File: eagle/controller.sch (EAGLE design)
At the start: 18 parts, among them IC2 74HCT595N

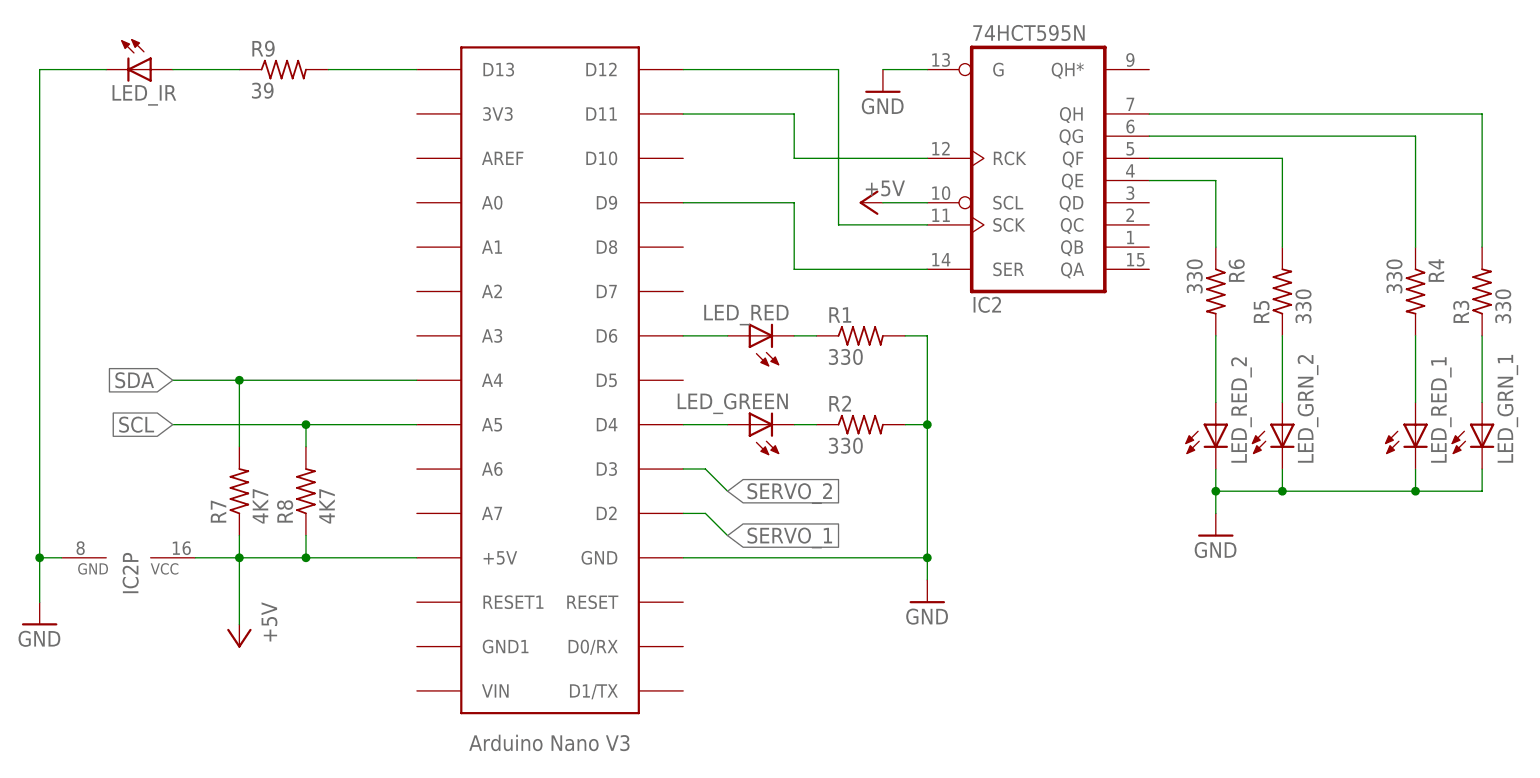
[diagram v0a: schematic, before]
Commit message: Clarify servo connections in schematic
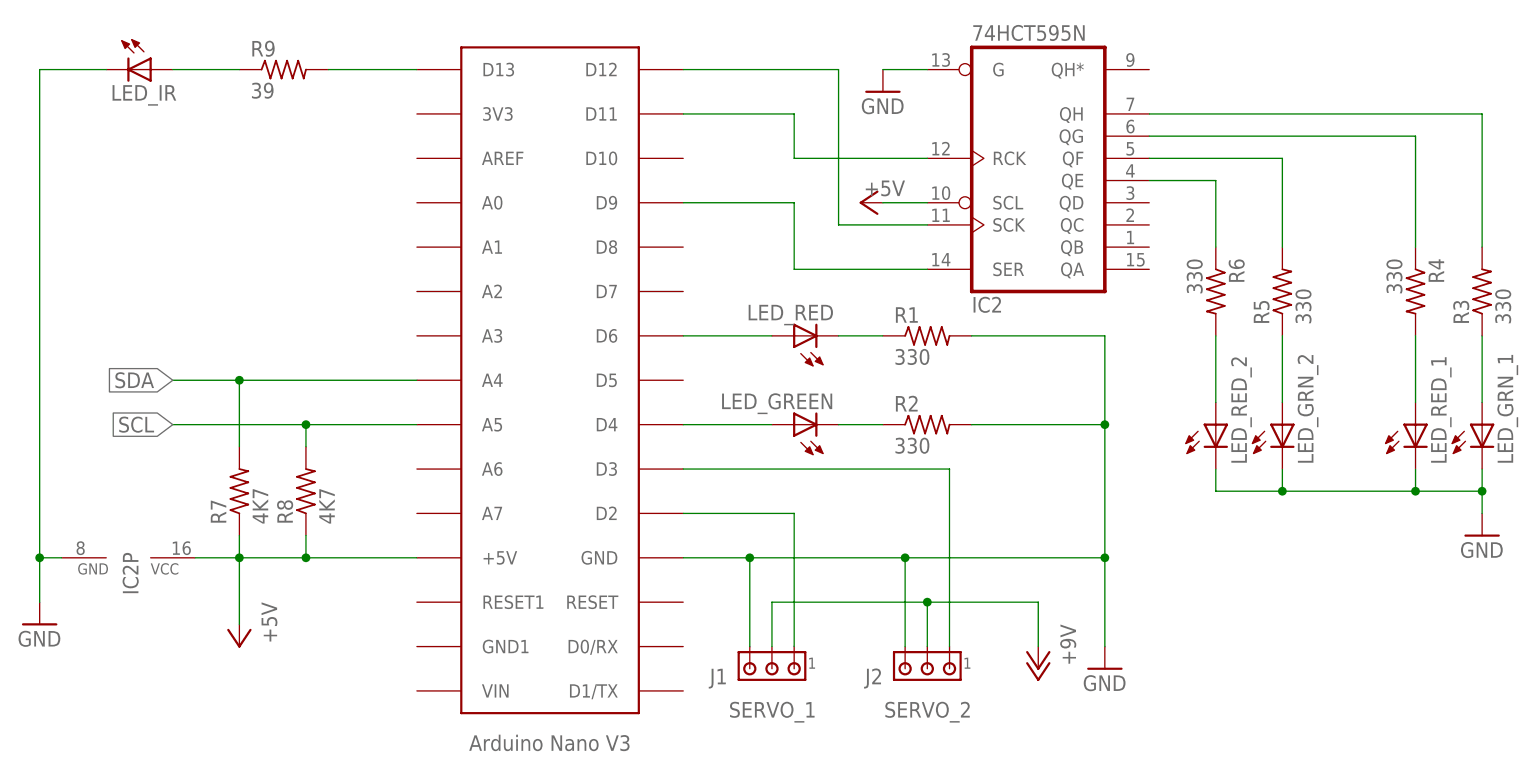
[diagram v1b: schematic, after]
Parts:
- added J1: SERVO_1, con-amp:MTA03-100
- added J2: SERVO_2, con-amp:MTA03-100
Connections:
- removed net SERVO_1: U$1.D2
- removed net SERVO_2: U$1.D3
- new net +12V: J1.2, J2.2
- new net N$18: J1.1, U$1.D2
- new net N$19: J2.1, U$1.D3
- net GND: now also J1.3, J2.3
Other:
- moved on the sheet: LED_GREEN, LED_RED, R1, R2
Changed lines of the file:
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@@
 <part name="R8" library="resistor" deviceset="R-US_" device="0207/10" value="4K7"/>
 <part name="P+1" library="supply1" deviceset="+5V" device=""/>
-<part name="GND3" library="supply1" deviceset="GND" device=""/>
 <part name="R9" library="resistor" deviceset="R-US_" device="0207/10" value="39"/>
 <part name="LED_IR" library="led" deviceset="LED" device="5MM"/>
@@
 <part name="GND1" library="supply1" deviceset="GND" device=""/>
 <part name="GND2" library="supply1" deviceset="GND" device=""/>
+<part name="J1" library="con-amp" deviceset="MTA03-100" device="" value="SERVO_1"/>
+<part name="J2" library="con-amp" deviceset="MTA03-100" device="" value="SERVO_2"/>
+<part name="P+3" library="supply1" deviceset="+12V" device="" value="+9V"/>
+<part name="GND4" library="supply1" deviceset="GND" device=""/>
 </parts>
 <sheets>
@@
 <attribute name="VALUE" x="-2.54" y="48.26" size="1.778" layer="96" rot="R180"/>
 </instance>
-<instance part="LED_GREEN" gate="G$1" x="-20.32" y="20.32" rot="R90"/>
-<instance part="LED_RED" gate="G$1" x="-20.32" y="30.48" rot="R90"/>
-<instance part="R1" gate="G$1" x="-7.62" y="30.48"/>
-<instance part="R2" gate="G$1" x="-7.62" y="20.32"/>
+<instance part="LED_GREEN" gate="G$1" x="-15.24" y="20.32" rot="R90"/>
+<instance part="LED_RED" gate="G$1" x="-15.24" y="30.48" rot="R90"/>
+<instance part="R1" gate="G$1" x="0" y="30.48"/>
+<instance part="R2" gate="G$1" x="0" y="20.32"/>
 <instance part="R3" gate="G$1" x="63.5" y="35.56" rot="R90"/>
 <instance part="R4" gate="G$1" x="55.88" y="35.56" rot="R270"/>
@@
 <instance part="R8" gate="G$1" x="-71.12" y="12.7" rot="R90"/>
 <instance part="P+1" gate="1" x="-78.74" y="-5.08" rot="R180"/>
-<instance part="GND3" gate="1" x="0" y="0"/>
 <instance part="R9" gate="G$1" x="-73.66" y="60.96"/>
 <instance part="LED_IR" gate="G$1" x="-88.9" y="60.96" rot="R270"/>
@@
 <instance part="LED_GRN_1" gate="G$1" x="63.5" y="20.32"/>
 <instance part="LED_GRN_2" gate="G$1" x="40.64" y="20.32"/>
-<instance part="GND5" gate="1" x="33.02" y="7.62"/>
+<instance part="GND5" gate="1" x="63.5" y="7.62"/>
 <instance part="IC2" gate="A" x="12.7" y="48.26" rot="MR180"/>
 <instance part="GND1" gate="1" x="-5.08" y="58.42"/>
 <instance part="IC2" gate="P" x="-91.44" y="5.08" rot="R270"/>
 <instance part="GND2" gate="1" x="-101.6" y="-2.54"/>
+<instance part="J1" gate="G$1" x="-17.78" y="-7.62" smashed="yes" rot="R180">
+<attribute name="NAME" x="-22.86" y="-7.62" size="1.778" layer="95" rot="R180"/>
+<attribute name="VALUE" x="-12.7" y="-11.43" size="1.778" layer="96" rot="R180"/>
+</instance>
+<instance part="J2" gate="G$1" x="0" y="-7.62" smashed="yes" rot="R180">
+<attribute name="NAME" x="-5.08" y="-7.62" size="1.778" layer="95" rot="R180"/>
+<attribute name="VALUE" x="5.08" y="-11.43" size="1.778" layer="96" rot="R180"/>
+</instance>
+<instance part="P+3" gate="1" x="12.7" y="-7.62" rot="R180"/>
+<instance part="GND4" gate="1" x="20.32" y="-7.62"/>
 </instances>
 <busses>
@@
 </net>
 <net name="GND" class="0">
-<segment>
-<pinref part="R1" gate="G$1" pin="2"/>
-<wire x1="-2.54" y1="30.48" x2="0" y2="30.48" width="0.1524" layer="91"/>
-<wire x1="0" y1="30.48" x2="0" y2="20.32" width="0.1524" layer="91"/>
-<pinref part="GND3" gate="1" pin="GND"/>
-<pinref part="R2" gate="G$1" pin="2"/>
-<wire x1="0" y1="20.32" x2="0" y2="5.08" width="0.1524" layer="91"/>
-<wire x1="0" y1="5.08" x2="0" y2="2.54" width="0.1524" layer="91"/>
-<wire x1="-2.54" y1="20.32" x2="0" y2="20.32" width="0.1524" layer="91"/>
-<junction x="0" y="20.32"/>
-<pinref part="U$1" gate="G$1" pin="GND"/>
-<wire x1="-27.94" y1="5.08" x2="0" y2="5.08" width="0.1524" layer="91"/>
-<junction x="0" y="5.08"/>
-</segment>
 <segment>
 <pinref part="LED_IR" gate="G$1" pin="C"/>
@@
 <wire x1="-101.6" y1="5.08" x2="-101.6" y2="0" width="0.1524" layer="91"/>
 <junction x="-101.6" y="5.08"/>
+</segment>
+<segment>
+<pinref part="IC2" gate="A" pin="G"/>
+<wire x1="0" y1="60.96" x2="-5.08" y2="60.96" width="0.1524" layer="91"/>
+<pinref part="GND1" gate="1" pin="GND"/>
+</segment>
+<segment>
+<pinref part="U$1" gate="G$1" pin="GND"/>
+<pinref part="J1" gate="G$1" pin="3"/>
+<wire x1="-20.32" y1="-5.08" x2="-20.32" y2="5.08" width="0.1524" layer="91"/>
+<wire x1="-20.32" y1="5.08" x2="-27.94" y2="5.08" width="0.1524" layer="91"/>
+<pinref part="J2" gate="G$1" pin="3"/>
+<wire x1="-2.54" y1="-5.08" x2="-2.54" y2="5.08" width="0.1524" layer="91"/>
+<wire x1="-2.54" y1="5.08" x2="-20.32" y2="5.08" width="0.1524" layer="91"/>
+<junction x="-20.32" y="5.08"/>
+<wire x1="-2.54" y1="5.08" x2="20.32" y2="5.08" width="0.1524" layer="91"/>
+<junction x="-2.54" y="5.08"/>
+<wire x1="20.32" y1="5.08" x2="20.32" y2="-5.08" width="0.1524" layer="91"/>
+<pinref part="GND4" gate="1" pin="GND"/>
+<pinref part="R1" gate="G$1" pin="2"/>
+<wire x1="5.08" y1="30.48" x2="20.32" y2="30.48" width="0.1524" layer="91"/>
+<wire x1="20.32" y1="30.48" x2="20.32" y2="20.32" width="0.1524" layer="91"/>
+<pinref part="R2" gate="G$1" pin="2"/>
+<wire x1="5.08" y1="20.32" x2="20.32" y2="20.32" width="0.1524" layer="91"/>
+<wire x1="20.32" y1="20.32" x2="20.32" y2="5.08" width="0.1524" layer="91"/>
+<junction x="20.32" y="20.32"/>
+<junction x="20.32" y="5.08"/>
 </segment>
 <segment>
@@
 <junction x="40.64" y="12.7"/>
 <pinref part="GND5" gate="1" pin="GND"/>
-<wire x1="33.02" y1="12.7" x2="33.02" y2="10.16" width="0.1524" layer="91"/>
-<junction x="33.02" y="12.7"/>
-</segment>
-<segment>
-<pinref part="IC2" gate="A" pin="G"/>
-<wire x1="0" y1="60.96" x2="-5.08" y2="60.96" width="0.1524" layer="91"/>
-<pinref part="GND1" gate="1" pin="GND"/>
+<wire x1="63.5" y1="10.16" x2="63.5" y2="12.7" width="0.1524" layer="91"/>
+<junction x="63.5" y="12.7"/>
 </segment>
 </net>
@@
 <pinref part="U$1" gate="G$1" pin="D4"/>
 <pinref part="LED_GREEN" gate="G$1" pin="A"/>
-<wire x1="-27.94" y1="20.32" x2="-22.86" y2="20.32" width="0.1524" layer="91"/>
+<wire x1="-27.94" y1="20.32" x2="-17.78" y2="20.32" width="0.1524" layer="91"/>
 </segment>
 </net>
@@
 <pinref part="U$1" gate="G$1" pin="D6"/>
 <pinref part="LED_RED" gate="G$1" pin="A"/>
-<wire x1="-27.94" y1="30.48" x2="-22.86" y2="30.48" width="0.1524" layer="91"/>
+<wire x1="-27.94" y1="30.48" x2="-17.78" y2="30.48" width="0.1524" layer="91"/>
 </segment>
 </net>
@@
 <pinref part="LED_RED" gate="G$1" pin="C"/>
 <pinref part="R1" gate="G$1" pin="1"/>
-<wire x1="-15.24" y1="30.48" x2="-12.7" y2="30.48" width="0.1524" layer="91"/>
+<wire x1="-10.16" y1="30.48" x2="-5.08" y2="30.48" width="0.1524" layer="91"/>
 </segment>
 </net>
@@
 <pinref part="LED_GREEN" gate="G$1" pin="C"/>
 <pinref part="R2" gate="G$1" pin="1"/>
-<wire x1="-15.24" y1="20.32" x2="-12.7" y2="20.32" width="0.1524" layer="91"/>
+<wire x1="-10.16" y1="20.32" x2="-5.08" y2="20.32" width="0.1524" layer="91"/>
 </segment>
 </net>
@@
 </segment>
 </net>
-<net name="SERVO_2" class="0">
-<segment>
-<pinref part="U$1" gate="G$1" pin="D3"/>
-<wire x1="-27.94" y1="15.24" x2="-25.4" y2="15.24" width="0.1524" layer="91"/>
-<wire x1="-25.4" y1="15.24" x2="-22.86" y2="12.7" width="0.1524" layer="91"/>
-<label x="-22.86" y="12.7" size="1.778" layer="95" xref="yes"/>
-</segment>
-</net>
-<net name="SERVO_1" class="0">
-<segment>
-<pinref part="U$1" gate="G$1" pin="D2"/>
-<wire x1="-27.94" y1="10.16" x2="-25.4" y2="10.16" width="0.1524" layer="91"/>
-<wire x1="-25.4" y1="10.16" x2="-22.86" y2="7.62" width="0.1524" layer="91"/>
-<label x="-22.86" y="7.62" size="1.778" layer="95" xref="yes"/>
-</segment>
-</net>
 <net name="N$8" class="0">
 <segment>
@@
 </segment>
 </net>
+<net name="N$18" class="0">
+<segment>
+<pinref part="U$1" gate="G$1" pin="D2"/>
+<wire x1="-27.94" y1="10.16" x2="-15.24" y2="10.16" width="0.1524" layer="91"/>
+<pinref part="J1" gate="G$1" pin="1"/>
+<wire x1="-15.24" y1="10.16" x2="-15.24" y2="-5.08" width="0.1524" layer="91"/>
+</segment>
+</net>
+<net name="N$19" class="0">
+<segment>
+<pinref part="U$1" gate="G$1" pin="D3"/>
+<wire x1="-27.94" y1="15.24" x2="2.54" y2="15.24" width="0.1524" layer="91"/>
+<pinref part="J2" gate="G$1" pin="1"/>
+<wire x1="2.54" y1="15.24" x2="2.54" y2="-5.08" width="0.1524" layer="91"/>
+</segment>
+</net>
+<net name="+12V" class="0">
+<segment>
+<pinref part="J1" gate="G$1" pin="2"/>
+<wire x1="-17.78" y1="-5.08" x2="-17.78" y2="0" width="0.1524" layer="91"/>
+<wire x1="-17.78" y1="0" x2="0" y2="0" width="0.1524" layer="91"/>
+<wire x1="0" y1="0" x2="12.7" y2="0" width="0.1524" layer="91"/>
+<wire x1="12.7" y1="0" x2="12.7" y2="-5.08" width="0.1524" layer="91"/>
+<pinref part="P+3" gate="1" pin="+12V"/>
+<pinref part="J2" gate="G$1" pin="2"/>
+<wire x1="0" y1="-5.08" x2="0" y2="0" width="0.1524" layer="91"/>
+<junction x="0" y="0"/>
+</segment>
+</net>
